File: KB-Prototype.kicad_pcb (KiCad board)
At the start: 2 copper layers, 145.3 x 57.2 mm, 45 parts, among them J1 Conn_01x04, J2 Conn_01x04, J3 Conn_01x04, SW1 SW_Push, U1 ATmega32U4-AU, Y1 Resonator_Small

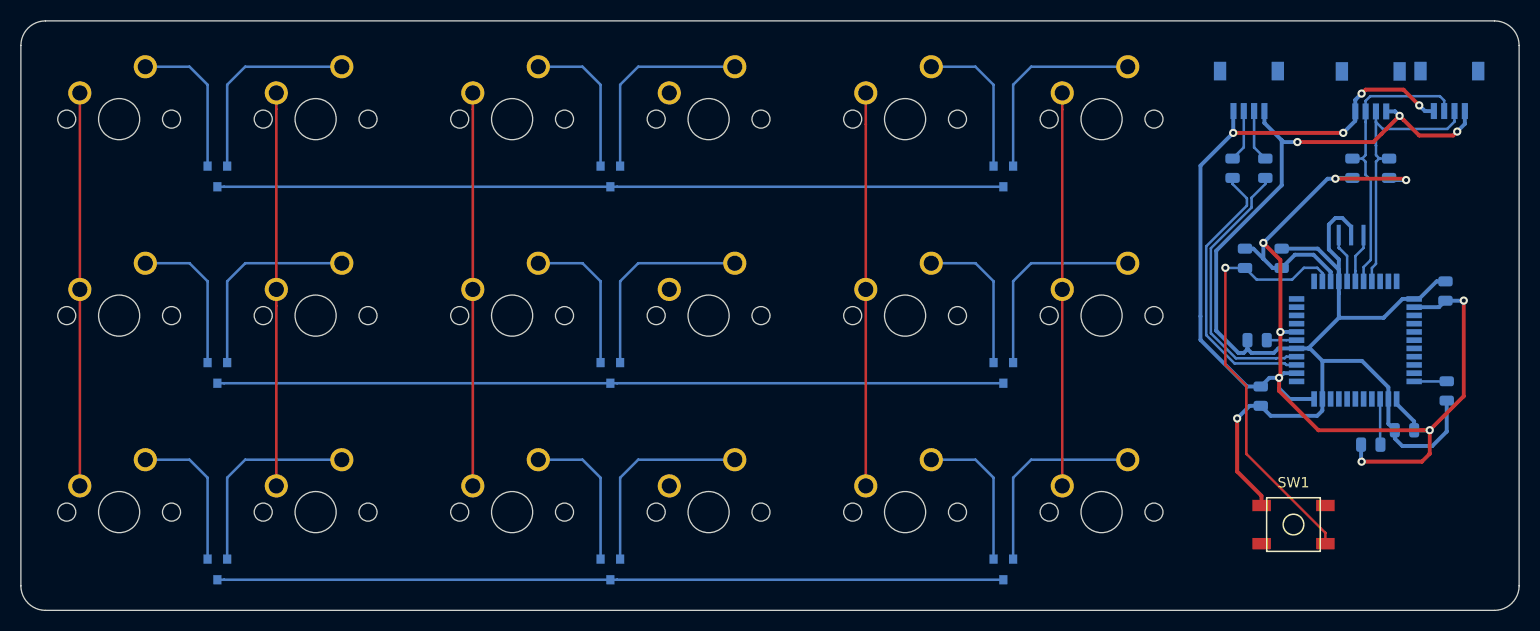
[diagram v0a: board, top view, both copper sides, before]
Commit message: hooked up cols/row, added silkscreen
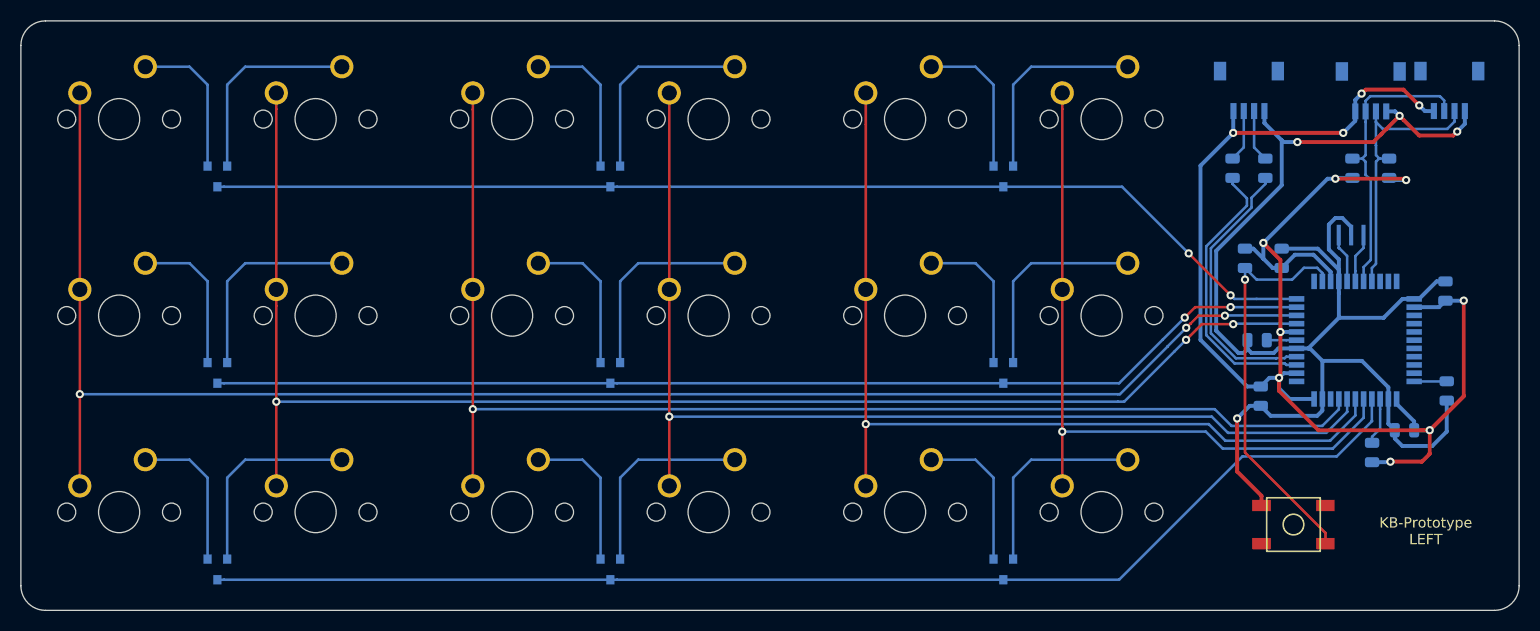
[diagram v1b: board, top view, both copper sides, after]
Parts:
- moved R7 0.77 mm to (154.8, 65.7), turned to 90 degrees
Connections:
- U1 pad 10: Net-(U1-Pad10) -> ROW1
- U1 pad 11: Net-(U1-Pad11) -> ROW0
- U1 pad 37: Net-(U1-Pad37) -> ROW2
- U1 pad 38: Net-(U1-Pad38) -> COL5
- U1 pad 39: Net-(U1-Pad39) -> COL4
- U1 pad 40: Net-(U1-Pad40) -> COL3
- U1 pad 41: Net-(U1-Pad41) -> COL2
- U1 pad 8: Net-(U1-Pad8) -> COL1
- U1 pad 9: Net-(U1-Pad9) -> COL0
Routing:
- net COL0: track 38.1 -> 159.5 mm, vias 0 -> 3
- net COL3: track 0.00 -> 106.7 mm, vias 0 -> 1
- net COL1: track 38.1 -> 140.3 mm, vias 0 -> 3
- net COL2: track 38.1 -> 124.5 mm, vias 0 -> 1
- net COL4: track 38.1 -> 89.0 mm, vias 0 -> 1
- net ROW2: track 76.2 -> 120.5 mm
- net COL5: track 38.1 -> 71.5 mm, vias 0 -> 1
- net ROW0: track 76.2 -> 109.1 mm, vias 0 -> 2
- net ROW1: track 76.2 -> 107.7 mm, vias 0 -> 2
- net Net-(R1-Pad2): track 42.1 -> 39.4 mm
- net +5V: track 163.9 -> 161.3 mm
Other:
- board text added: "JLCJLCJLCJLC"
- board text added: "KB-Prototype LEFT"

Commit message: added mounting holes
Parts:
- added H1: MountingHole, random-keyboard-parts:Generic-Mounthole, F.Cu at (26.8, 26.7)
- added H2: MountingHole, random-keyboard-parts:Generic-Mounthole, F.Cu at (26.7, 78.1)
- added H3: MountingHole, random-keyboard-parts:Generic-Mounthole, F.Cu at (165.9, 37.6)
- added H4: MountingHole, random-keyboard-parts:Generic-Mounthole, F.Cu at (165.9, 77.9)
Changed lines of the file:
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@@
     (tracks 403)
     (zones 0)
-    (modules 45)
+    (modules 49)
     (nets 56)
   )
@@
     (solder_mask_min_width 0.25)
     (aux_axis_origin 0 0)
-    (visible_elements 7FFFEFFF)
+    (visible_elements 7FFFFFFF)
     (pcbplotparams
       (layerselection 0x010fc_ffffffff)
@@
     (add_net GND)
   )
+  (module random-keyboard-parts:Generic-Mounthole (layer F.Cu)
+    (at 165.862 77.851)
+    (attr virtual)
+    (fp_text reference H4 (at 0 2) (layer Dwgs.User)
+      (effects (font (size 1 1) (thickness 0.15)))
+    )
+    (fp_text value MountingHole (at 0 -2) (layer Dwgs.User)
+      (effects (font (size 1 1) (thickness 0.15)))
+    )
+    (pad 1 thru_hole circle (at 0 0) (size 3.5 3.5) (drill 2.2) (layers *.Cu *.Mask))
+  )
+  (module random-keyboard-parts:Generic-Mounthole (layer F.Cu)
+    (at 165.862 37.592)
+    (attr virtual)
+    (fp_text reference H3 (at 0 2) (layer Dwgs.User)
+      (effects (font (size 1 1) (thickness 0.15)))
+    )
+    (fp_text value MountingHole (at 0 -2) (layer Dwgs.User)
+      (effects (font (size 1 1) (thickness 0.15)))
+    )
+    (pad 1 thru_hole circle (at 0 0) (size 3.5 3.5) (drill 2.2) (layers *.Cu *.Mask))
+  )
+  (module random-keyboard-parts:Generic-Mounthole (layer F.Cu)
+    (at 26.67 78.105)
+    (attr virtual)
+    (fp_text reference H2 (at 0 2) (layer Dwgs.User)
+      (effects (font (size 1 1) (thickness 0.15)))
+    )
+    (fp_text value MountingHole (at 0 -2) (layer Dwgs.User)
+      (effects (font (size 1 1) (thickness 0.15)))
+    )
+    (pad 1 thru_hole circle (at 0 0) (size 3.5 3.5) (drill 2.2) (layers *.Cu *.Mask))
+  )
+  (module random-keyboard-parts:Generic-Mounthole (layer F.Cu)
+    (at 26.797 26.67)
+    (attr virtual)
+    (fp_text reference H1 (at 0 2) (layer Dwgs.User)
+      (effects (font (size 1 1) (thickness 0.15)))
+    )
+    (fp_text value MountingHole (at 0 -2) (layer Dwgs.User)
+      (effects (font (size 1 1) (thickness 0.15)))
+    )
+    (pad 1 thru_hole circle (at 0 0) (size 3.5 3.5) (drill 2.2) (layers *.Cu *.Mask))
+  )
   (module DIMR_Keyboard_Parts:CSTCE (layer B.Cu)

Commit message: generated gerbers
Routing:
- added copper zone on B.Cu, net GND
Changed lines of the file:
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@@
     (solder_mask_min_width 0.25)
     (aux_axis_origin 0 0)
-    (visible_elements 7FFFFFFF)
+    (visible_elements 7FFFEFFF)
     (pcbplotparams
-      (layerselection 0x010fc_ffffffff)
-      (usegerberextensions false)
+      (layerselection 0x010f0_ffffffff)
+      (usegerberextensions true)
       (usegerberattributes false)
       (usegerberadvancedattributes false)
@@
       (plotinvisibletext false)
       (padsonsilk false)
-      (subtractmaskfromsilk false)
+      (subtractmaskfromsilk true)
       (outputformat 1)
       (mirror false)
-      (drillshape 1)
+      (drillshape 0)
       (scaleselection 1)
-      (outputdirectory ""))
+      (outputdirectory "Gerbers"))
   )
   (net 0 "")
@@
   (segment (start 151.601 45.847) (end 151.581 45.827) (width 0.25) (layer B.Cu) (net 53))
   (segment (start 151.638 45.847) (end 151.601 45.847) (width 0.25) (layer B.Cu) (net 53))
+  (zone (net 1) (net_name GND) (layer B.Cu) (hatch edge 0.508)
+    (connect_pads (clearance 0.508))
+    (min_thickness 0.254)
+    (fill yes (arc_segments 32) (thermal_gap 0.508) (thermal_bridge_width 0.508) (smoothing chamfer) (radius 0.5))
+    (polygon
+      (pts
+        (xy 147.955 49.53) (xy 147.955 60.071) (xy 158.496 60.071) (xy 158.496 49.53)
+      )
+    )
+  )
 )
